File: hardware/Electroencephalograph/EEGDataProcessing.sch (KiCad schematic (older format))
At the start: 23 parts, among them J3 Conn_01x04_Female, J4 Conn_01x04_Female, U3 STM32F030K6Tx, Y1 20MHz

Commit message: further routing
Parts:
- removed TP14, TP15, TP16, TP8: TestPoint, TestPoint:TestPoint_Pad_D1.0mm, symbol Connector:TestPoint
- added U11: GD25D10BOIGR, Package_SO:TSSOP-8_4.4x3mm_P0.65mm, symbol Electroencephalograph:GD25D10BOIGR
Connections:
- net labels added: CS, MISO, MOSI, SCK
- net labels removed: FSELECT, FSYNC, PSEL0, PSEL1, REL_1, REL_2, REL_3, ROT_A, ROT_B, ROT_S, SPI1_CS_AMPLIFIER, SPI1_MOSI, SPI1_SCK
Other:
- note removed: "5v -> 3v3"
- note removed: "test points for spi"
- moved on the sheet: C104, J3, J4, R75, R76, R77

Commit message: placement of usb interface, fix in grounds
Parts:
- removed U11: GD25D10BOIGR, Package_SO:TSSOP-8_4.4x3mm_P0.65mm, symbol Electroencephalograph:GD25D10BOIGR
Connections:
- net labels added: DP_GND
- net labels removed: GND
- no-connect marks 1 -> 13
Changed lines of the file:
@@
 encoding utf-8
 Sheet 4 8
-Title ""
+Title "EEG signal processing"
 Date ""
-Rev ""
-Comp ""
+Rev "1.0"
+Comp "MIT License"
 Comment1 ""
 Comment2 ""
@@
 	4850 2700 4850 2650
 $Comp
-L power:GND #PWR?
+L Electroencephalograph:DP_GND #PWR?
 U 1 1 5DC51E49
 P 4850 2700
@@
 AR Path="/5E142744/5DC51E49" Ref="#PWR0185"  Part="1"
 F 0 "#PWR0185" H 4850 2450 50  0001 C CNN
-F 1 "GND" H 4855 2527 50  0000 C CNN
+F 1 "DP_GND" H 4855 2527 50  0000 C CNN
 F 2 "" H 4850 2700 50  0001 C CNN
 F 3 "" H 4850 2700 50  0001 C CNN
@@
 $EndComp
 $Comp
-L power:GND #PWR?
+L Electroencephalograph:DP_GND #PWR?
 U 1 1 5DDA3F66
 P 3650 4950
@@
 AR Path="/5E142744/5DDA3F66" Ref="#PWR0182"  Part="1"
 F 0 "#PWR0182" H 3650 4700 50  0001 C CNN
-F 1 "GND" H 3655 4777 50  0000 C CNN
+F 1 "DP_GND" H 3655 4777 50  0000 C CNN
 F 2 "" H 3650 4950 50  0001 C CNN
 F 3 "" H 3650 4950 50  0001 C CNN
@@
 	4050 2700 4050 2650
 $Comp
-L power:GND #PWR?
+L Electroencephalograph:DP_GND #PWR?
 U 1 1 5E0D2F09
 P 4050 2700
@@
 AR Path="/5E142744/5E0D2F09" Ref="#PWR0183"  Part="1"
 F 0 "#PWR0183" H 4050 2450 50  0001 C CNN
-F 1 "GND" H 4055 2527 50  0000 C CNN
+F 1 "DP_GND" H 4055 2527 50  0000 C CNN
 F 2 "" H 4050 2700 50  0001 C CNN
 F 3 "" H 4050 2700 50  0001 C CNN
@@
 	5650 2700 5650 2650
 $Comp
-L power:GND #PWR?
+L Electroencephalograph:DP_GND #PWR?
 U 1 1 5E0D4A69
 P 5650 2700
@@
 AR Path="/5E142744/5E0D4A69" Ref="#PWR0187"  Part="1"
 F 0 "#PWR0187" H 5650 2450 50  0001 C CNN
-F 1 "GND" H 5655 2527 50  0000 C CNN
+F 1 "DP_GND" H 5655 2527 50  0000 C CNN
 F 2 "" H 5650 2700 50  0001 C CNN
 F 3 "" H 5650 2700 50  0001 C CNN
@@
 	4450 2700 4450 2650
 $Comp
-L power:GND #PWR?
+L Electroencephalograph:DP_GND #PWR?
 U 1 1 5E0F5071
 P 4450 2700
@@
 AR Path="/5E142744/5E0F5071" Ref="#PWR0184"  Part="1"
 F 0 "#PWR0184" H 4450 2450 50  0001 C CNN
-F 1 "GND" H 4455 2527 50  0000 C CNN
+F 1 "DP_GND" H 4455 2527 50  0000 C CNN
 F 2 "" H 4450 2700 50  0001 C CNN
 F 3 "" H 4450 2700 50  0001 C CNN
@@
 	5250 2700 5250 2650
 $Comp
-L power:GND #PWR?
+L Electroencephalograph:DP_GND #PWR?
 U 1 1 5E0F8553
 P 5250 2700
@@
 AR Path="/5E142744/5E0F8553" Ref="#PWR0186"  Part="1"
 F 0 "#PWR0186" H 5250 2450 50  0001 C CNN
-F 1 "GND" H 5255 2527 50  0000 C CNN
+F 1 "DP_GND" H 5255 2527 50  0000 C CNN
 F 2 "" H 5250 2700 50  0001 C CNN
 F 3 "" H 5250 2700 50  0001 C CNN
@@
 $EndComp
 $Comp
-L power:GND #PWR?
+L Electroencephalograph:DP_GND #PWR?
 U 1 1 5E1043B2
 P 6250 2700
@@
 AR Path="/5E142744/5E1043B2" Ref="#PWR0188"  Part="1"
 F 0 "#PWR0188" H 6250 2450 50  0001 C CNN
-F 1 "GND" H 6255 2527 50  0000 C CNN
+F 1 "DP_GND" H 6255 2527 50  0000 C CNN
 F 2 "" H 6250 2700 50  0001 C CNN
 F 3 "" H 6250 2700 50  0001 C CNN
@@
 	2000 3800 2050 3800
 $Comp
-L power:GND #PWR?
+L Electroencephalograph:DP_GND #PWR?
 U 1 1 5E11C657
 P 2050 4100
@@
 AR Path="/5E142744/5E11C657" Ref="#PWR0180"  Part="1"
 F 0 "#PWR0180" H 2050 3850 50  0001 C CNN
-F 1 "GND" H 2055 3927 50  0000 C CNN
+F 1 "DP_GND" H 2055 3927 50  0000 C CNN
 F 2 "" H 2050 4100 50  0001 C CNN
 F 3 "" H 2050 4100 50  0001 C CNN
@@
 $EndComp
 $Comp
-L power:GND #PWR?
+L Electroencephalograph:DP_GND #PWR?
 U 1 1 5E11C32E
 P 1550 4100
@@
 AR Path="/5E142744/5E11C32E" Ref="#PWR0179"  Part="1"
 F 0 "#PWR0179" H 1550 3850 50  0001 C CNN
-F 1 "GND" H 1555 3927 50  0000 C CNN
+F 1 "DP_GND" H 1555 3927 50  0000 C CNN
 F 2 "" H 1550 4100 50  0001 C CNN
 F 3 "" H 1550 4100 50  0001 C CNN
@@
 $EndComp
 $Comp
-L power:GND #PWR?
+L Electroencephalograph:DP_GND #PWR?
 U 1 1 5DC9B8ED
 P 1000 3850
@@
 AR Path="/5E142744/5DC9B8ED" Ref="#PWR0178"  Part="1"
 F 0 "#PWR0178" H 1000 3600 50  0001 C CNN
-F 1 "GND" H 1005 3677 50  0000 C CNN
+F 1 "DP_GND" H 1005 3677 50  0000 C CNN
 F 2 "" H 1000 3850 50  0001 C CNN
 F 3 "" H 1000 3850 50  0001 C CNN
@@
 USART_RX
 $Comp
-L power:GND #PWR?
+L Electroencephalograph:DP_GND #PWR?
 U 1 1 5E09BA01
 P 1700 7350
@@
 AR Path="/5E142744/5E09BA01" Ref="#PWR0191"  Part="1"
 F 0 "#PWR0191" H 1700 7100 50  0001 C CNN
-F 1 "GND" H 1705 7177 50  0000 C CNN
+F 1 "DP_GND" H 1705 7177 50  0000 C CNN
 F 2 "" H 1700 7350 50  0001 C CNN
 F 3 "" H 1700 7350 50  0001 C CNN
@@
 $EndComp
 $Comp
-L power:GND #PWR?
+L Electroencephalograph:DP_GND #PWR?
 U 1 1 5E141D24
 P 3750 7450
@@
 AR Path="/5E142744/5E141D24" Ref="#PWR0190"  Part="1"
 F 0 "#PWR0190" H 3750 7200 50  0001 C CNN
-F 1 "GND" H 3755 7277 50  0000 C CNN
+F 1 "DP_GND" H 3755 7277 50  0000 C CNN
 F 2 "" H 3750 7450 50  0001 C CNN
 F 3 "" H 3750 7450 50  0001 C CNN
@@
 $EndComp
 $Comp
-L power:GND #PWR?
+L Electroencephalograph:DP_GND #PWR?
 U 1 1 5E15BA17
 P 2400 3500
@@
 AR Path="/5E142744/5E15BA17" Ref="#PWR0181"  Part="1"
 F 0 "#PWR0181" H 2400 3250 50  0001 C CNN
-F 1 "GND" H 2405 3327 50  0000 C CNN
+F 1 "DP_GND" H 2405 3327 50  0000 C CNN
 F 2 "" H 2400 3500 50  0001 C CNN
 F 3 "" H 2400 3500 50  0001 C CNN
@@
 $EndComp
 $Comp
-L power:GND #PWR?
+L Electroencephalograph:DP_GND #PWR?
 U 1 1 5E17610B
 P 3500 7450
@@
 AR Path="/5E142744/5E17610B" Ref="#PWR0189"  Part="1"
 F 0 "#PWR0189" H 3500 7200 50  0001 C CNN
-F 1 "GND" H 3505 7277 50  0000 C CNN
+F 1 "DP_GND" H 3505 7277 50  0000 C CNN
 F 2 "" H 3500 7450 50  0001 C CNN
 F 3 "" H 3500 7450 50  0001 C CNN
@@
 Text GLabel 4900 3750 2    50   Output ~ 0
 MISO
-$Comp
-L Electroencephalograph:GD25D10BOIGR U11
-U 1 1 5E308455
-P 7950 3000
-F 0 "U11" H 7925 3075 50  0000 C CNN
-F 1 "GD25D10BOIGR" H 7925 2984 50  0000 C CNN
-F 2 "Package_SO:TSSOP-8_4.4x3mm_P0.65mm" H 7950 3000 50  0001 C CNN
-F 3 "" H 7950 3000 50  0001 C CNN
-	1    7950 3000
-	1    0    0    -1
-$EndComp
+NoConn ~ 4900 4350
+NoConn ~ 4900 4250
+NoConn ~ 4900 3950
+NoConn ~ 4900 3550
+NoConn ~ 4900 3450
+NoConn ~ 4900 3350
+NoConn ~ 4900 3250
+NoConn ~ 4900 3150
+NoConn ~ 2900 4450
+NoConn ~ 2900 4350
+NoConn ~ 2900 4250
+NoConn ~ 2900 4150
 $EndSCHEMATC

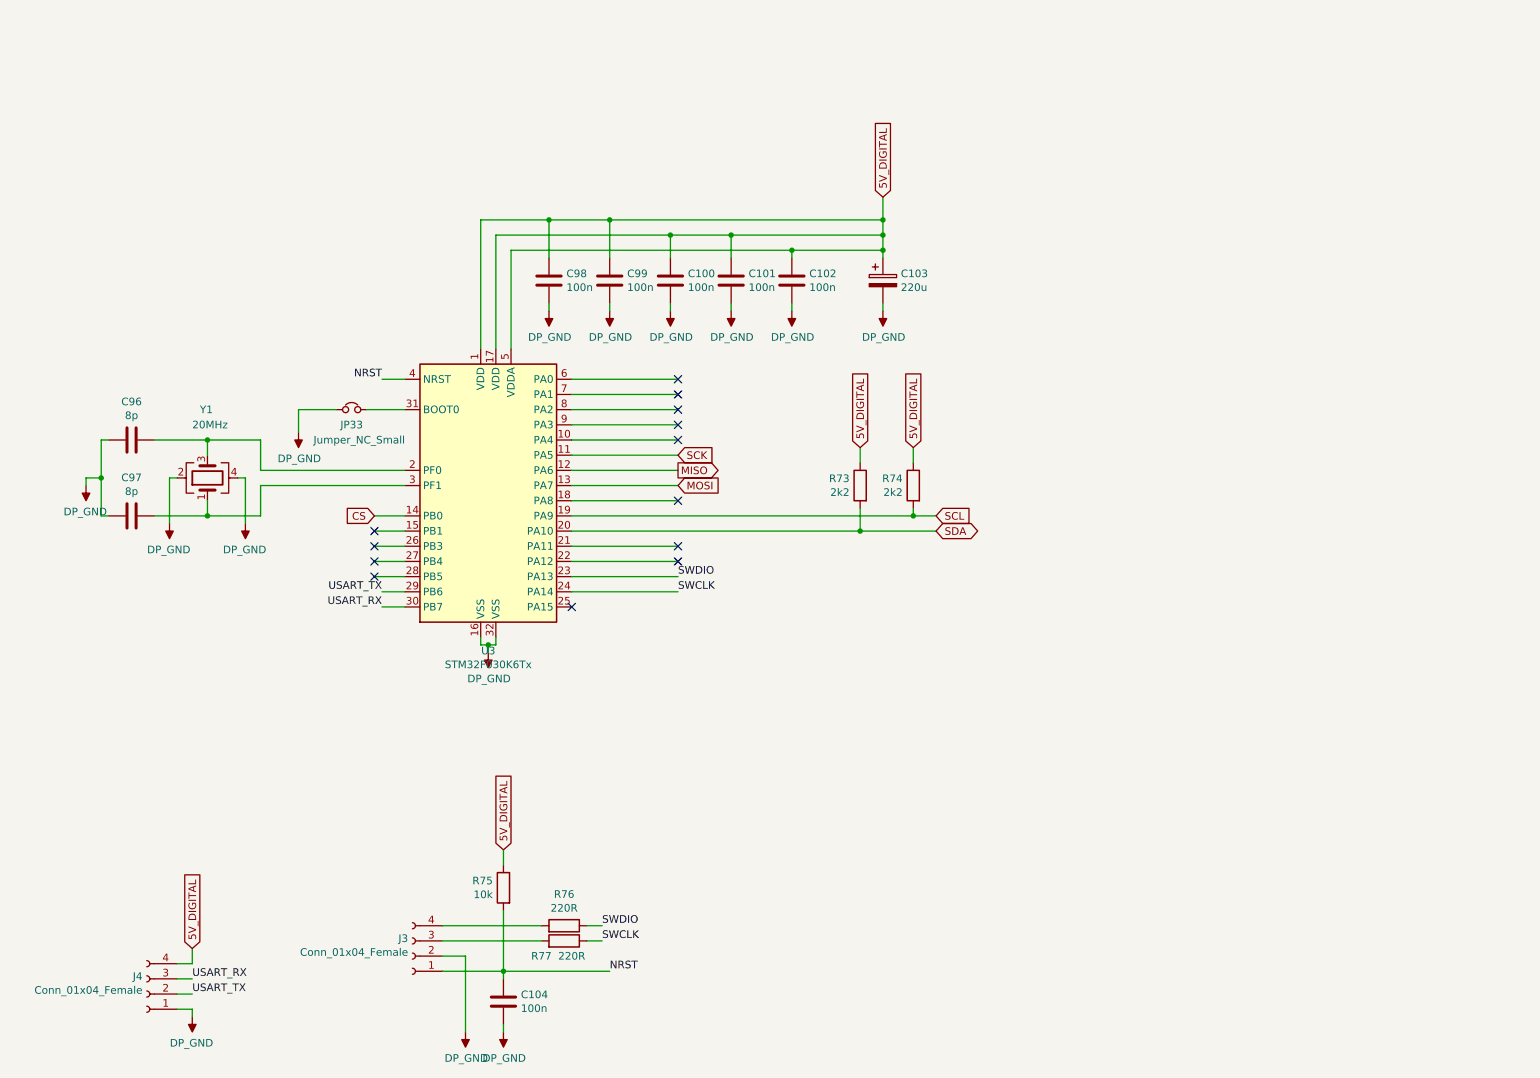
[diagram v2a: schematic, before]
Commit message: fix #41, fix #18
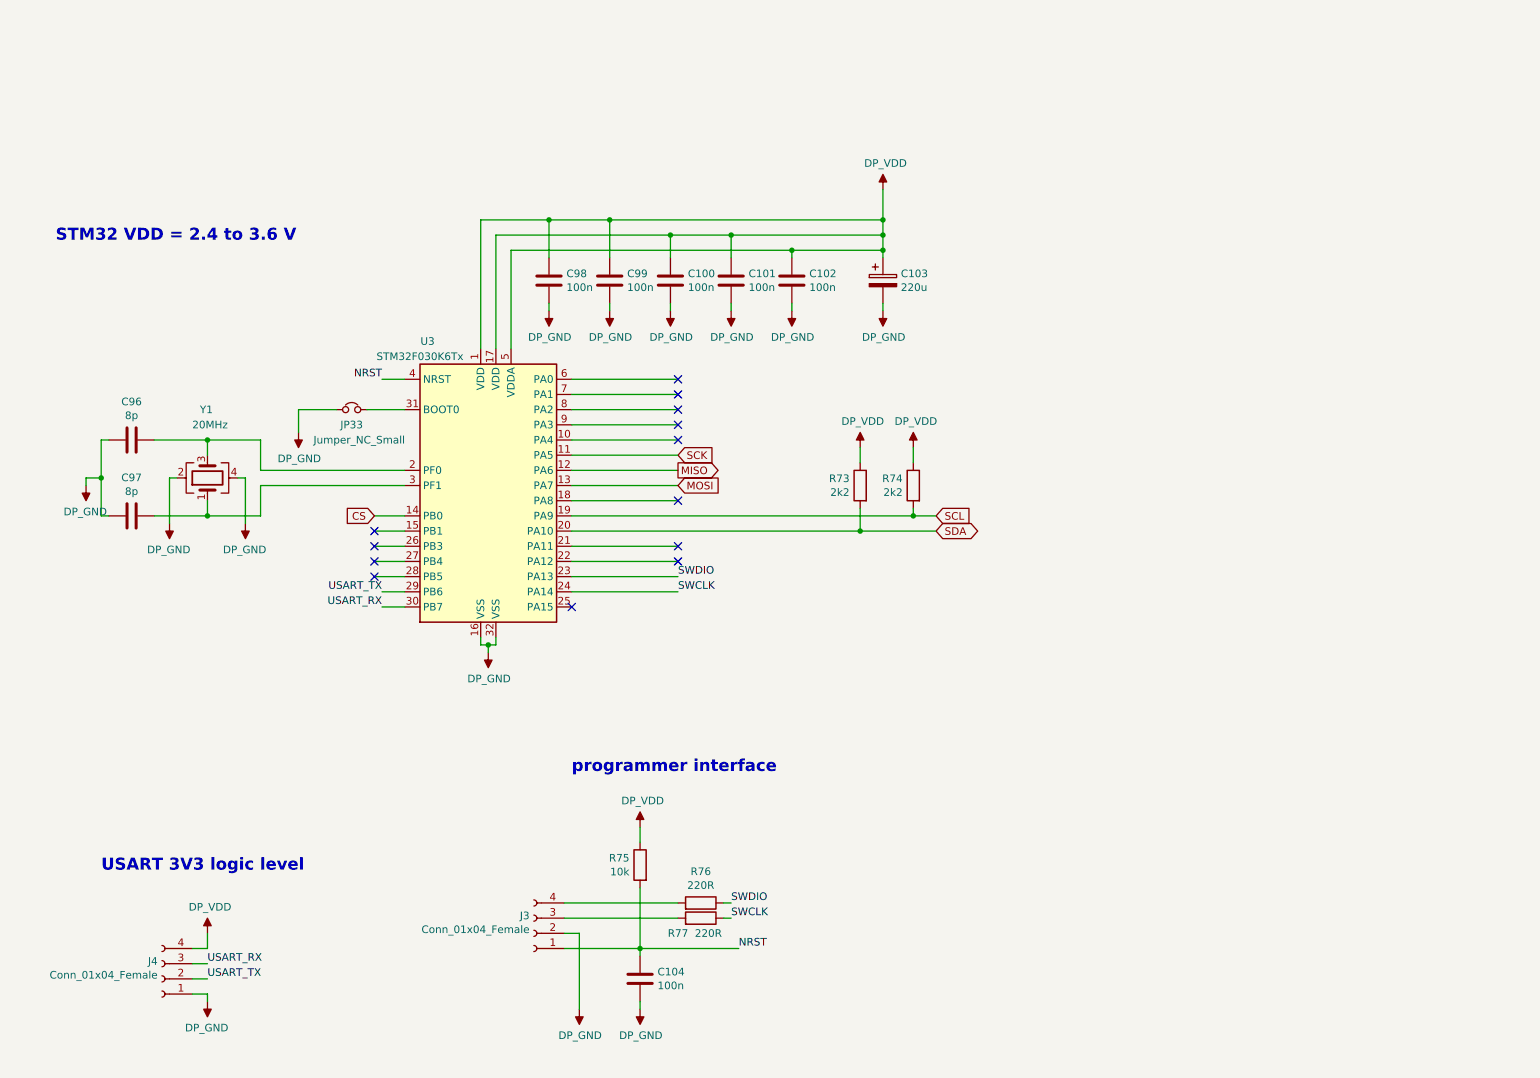
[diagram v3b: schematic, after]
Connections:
- net 5V_DIGITAL renamed DP_VDD
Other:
- note added: "STM32 VDD = 2.4 to 3.6 V"
- note added: "USART 3V3 logic level"
- note added: "programmer interface"
- moved on the sheet: C104, J3, J4, R75, R76, R77

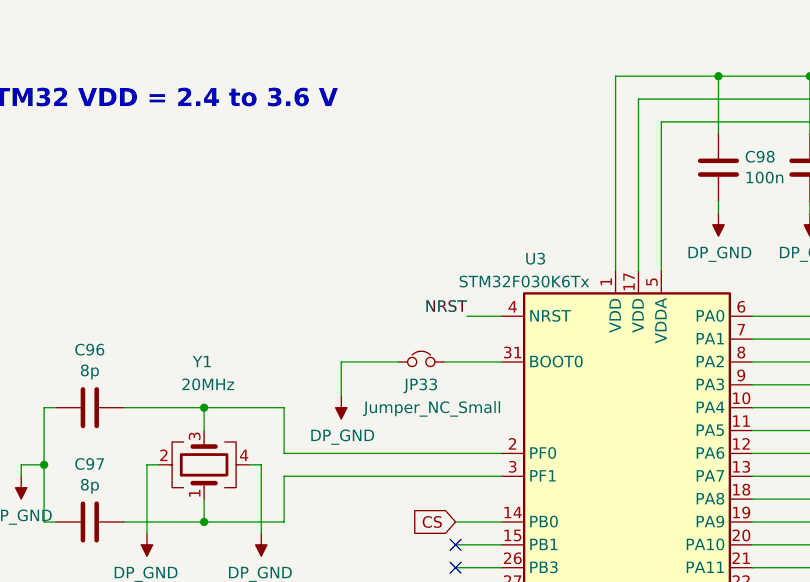
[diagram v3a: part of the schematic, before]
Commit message: fix for BOOT pin for MCU
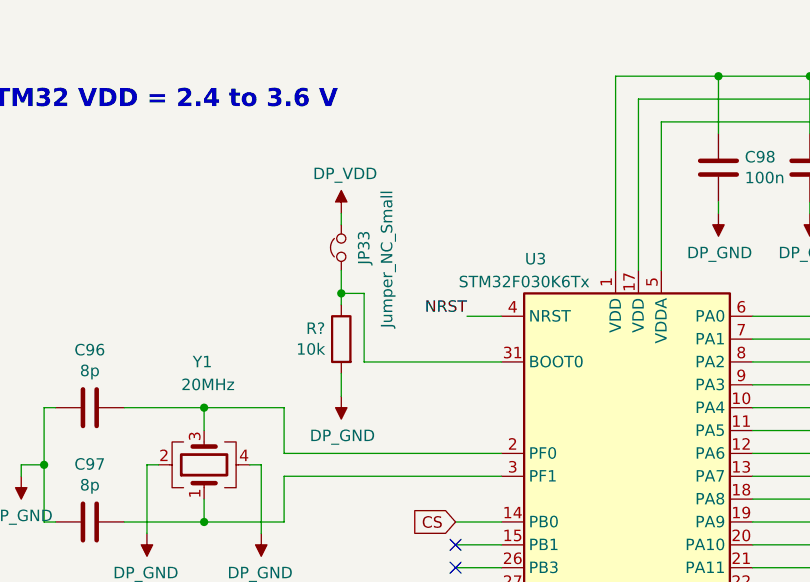
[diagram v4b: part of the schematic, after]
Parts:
- added R?: 10k, Resistor_SMD:R_0805_2012Metric_Pad1.15x1.40mm_HandSolder, symbol Device:R
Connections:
- net DP_GND: now also R?.2; no longer JP33.1
- net DP_VDD: now also JP33.1
- net at JP33.2, U3.31 (BOOT0): now also R?.1
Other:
- moved on the sheet: JP33
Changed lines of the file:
@@
 EESchema Schematic File Version 4
-LIBS:Electroencephalograph-cache
-EELAYER 29 0
+EELAYER 30 0
 EELAYER END
 $Descr A4 11693 8268
@@
 L Device:Jumper_NC_Small JP33
 U 1 1 5E15735A
-P 2750 3350
-F 0 "JP33" H 2750 3250 50  0000 C CNN
-F 1 "Jumper_NC_Small" H 2800 3150 50  0000 C CNN
-F 2 "Jumper:SolderJumper-2_P1.3mm_Bridged2Bar_RoundedPad1.0x1.5mm" H 2750 3350 50  0001 C CNN
-F 3 "~" H 2750 3350 50  0001 C CNN
-	1    2750 3350
-	1    0    0    -1
+P 2400 2850
+F 0 "JP33" H 2400 2750 50  0000 C CNN
+F 1 "Jumper_NC_Small" H 2450 2650 50  0000 C CNN
+F 2 "Jumper:SolderJumper-2_P1.3mm_Bridged2Bar_RoundedPad1.0x1.5mm" H 2400 2850 50  0001 C CNN
+F 3 "~" H 2400 2850 50  0001 C CNN
+	1    2400 2850
+	0    -1   1    0
 $EndComp
 $Comp
@@
 	1    0    0    -1
 $EndComp
-Wire Wire Line
-	3100 3350 2850 3350
-Wire Wire Line
-	2650 3350 2400 3350
-Wire Wire Line
-	2400 3350 2400 3500
 Text Label 2950 3150 2    50   ~ 0
 NRST
@@
 Text Notes 4200 5750 0    79   ~ 16
 programmer interface
+$Comp
+L Device:R R?
+U 1 1 5F015EE7
+P 2400 3250
+AR Path="/5F015EE7" Ref="R?"  Part="1"
+AR Path="/5DAEEEF4/5F015EE7" Ref="R?"  Part="1"
+AR Path="/5DD5C7F6/5F015EE7" Ref="R?"  Part="1"
+AR Path="/5E142744/5F015EE7" Ref="R?"  Part="1"
+F 0 "R?" H 2470 3296 50  0000 L CNN
+F 1 "10k" H 2470 3205 50  0000 L CNN
+F 2 "Resistor_SMD:R_0805_2012Metric_Pad1.15x1.40mm_HandSolder" V 2330 3250 50  0001 C CNN
+F 3 "~" H 2400 3250 50  0001 C CNN
+	1    2400 3250
+	-1   0    0    -1
+$EndComp
+$Comp
+L Electroencephalograph:DP_VDD #PWR?
+U 1 1 5F01C0B4
+P 2400 2700
+F 0 "#PWR?" H 2400 2825 50  0001 C CNN
+F 1 "DP_VDD" H 2417 2873 50  0000 C CNN
+F 2 "" H 2400 2825 50  0001 C CNN
+F 3 "" H 2400 2825 50  0001 C CNN
+	1    2400 2700
+	1    0    0    -1
+$EndComp
+Wire Wire Line
+	2400 2700 2400 2750
+Wire Wire Line
+	2400 2950 2400 3050
+Wire Wire Line
+	2400 3400 2400 3500
+Wire Wire Line
+	2500 3350 2500 3050
+Wire Wire Line
+	2500 3050 2400 3050
+Wire Wire Line
+	2500 3350 3100 3350
+Connection ~ 2400 3050
+Wire Wire Line
+	2400 3050 2400 3100
 $EndSCHEMATC

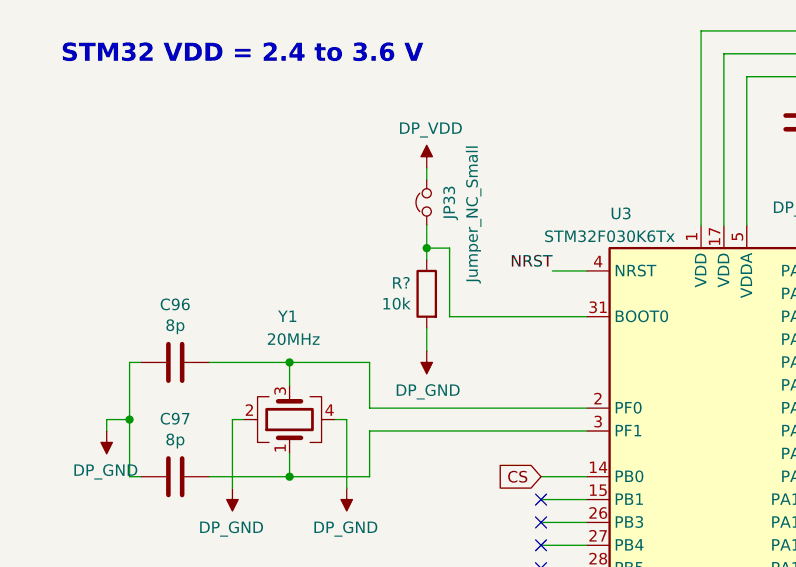
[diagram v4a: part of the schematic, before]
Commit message: add support for esp module
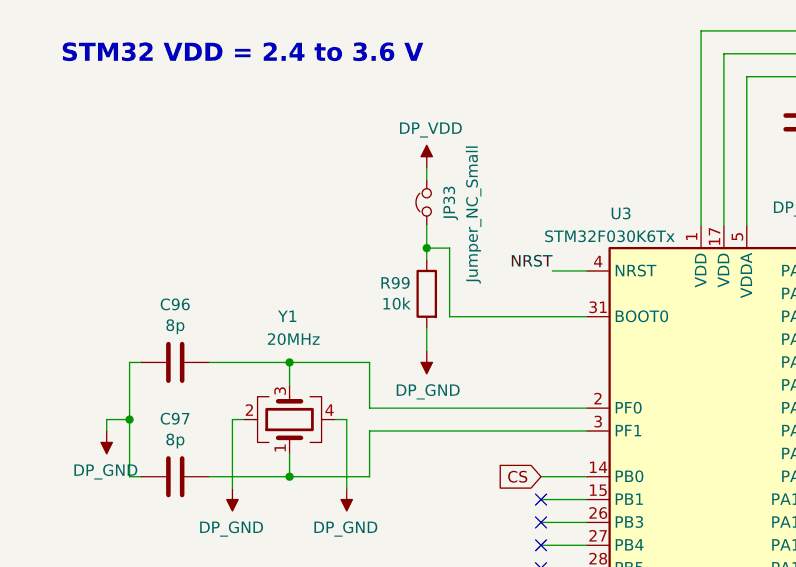
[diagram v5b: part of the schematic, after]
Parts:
- R73: footprint Resistor_SMD:R_0805_2012Metric_Pad1.15x1.40mm_HandSolder -> Resistor_SMD:R_0402_1005Metric
- R99: renamed from R?; footprint Resistor_SMD:R_0805_2012Metric_Pad1.15x1.40mm_HandSolder -> Resistor_SMD:R_0402_1005Metric
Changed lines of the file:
@@
 F 0 "R73" H 6170 3896 50  0000 L CNN
 F 1 "2k2" H 6170 3805 50  0000 L CNN
-F 2 "Resistor_SMD:R_0805_2012Metric_Pad1.15x1.40mm_HandSolder" V 6030 3850 50  0001 C CNN
+F 2 "Resistor_SMD:R_0402_1005Metric" V 6030 3850 50  0001 C CNN
 F 3 "~" H 6100 3850 50  0001 C CNN
 	1    6100 3850
@@
 AR Path="/5DAEEEF4/5F015EE7" Ref="R?"  Part="1"
 AR Path="/5DD5C7F6/5F015EE7" Ref="R?"  Part="1"
-AR Path="/5E142744/5F015EE7" Ref="R?"  Part="1"
-F 0 "R?" H 2470 3296 50  0000 L CNN
+AR Path="/5E142744/5F015EE7" Ref="R99"  Part="1"
+F 0 "R99" H 2470 3296 50  0000 L CNN
 F 1 "10k" H 2470 3205 50  0000 L CNN
-F 2 "Resistor_SMD:R_0805_2012Metric_Pad1.15x1.40mm_HandSolder" V 2330 3250 50  0001 C CNN
+F 2 "Resistor_SMD:R_0402_1005Metric" V 2330 3250 50  0001 C CNN
 F 3 "~" H 2400 3250 50  0001 C CNN
 	1    2400 3250
@@
 $EndComp
 $Comp
-L Electroencephalograph:DP_VDD #PWR?
+L Electroencephalograph:DP_VDD #PWR219
 U 1 1 5F01C0B4
 P 2400 2700
-F 0 "#PWR?" H 2400 2825 50  0001 C CNN
+F 0 "#PWR219" H 2400 2825 50  0001 C CNN
 F 1 "DP_VDD" H 2417 2873 50  0000 C CNN
 F 2 "" H 2400 2825 50  0001 C CNN
